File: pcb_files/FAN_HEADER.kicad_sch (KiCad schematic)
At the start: 6 parts

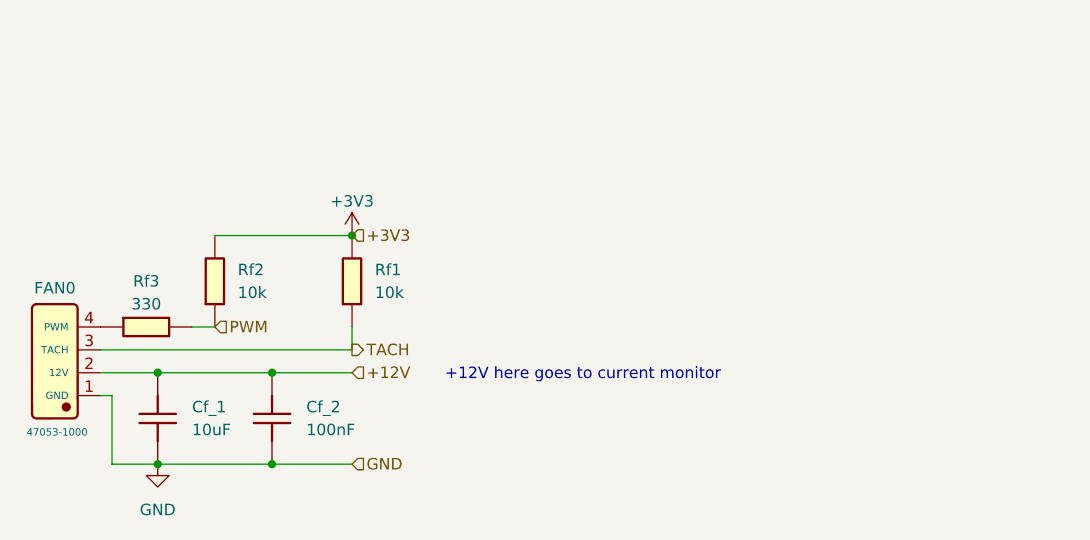
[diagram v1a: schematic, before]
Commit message: Added ESD protection to fans
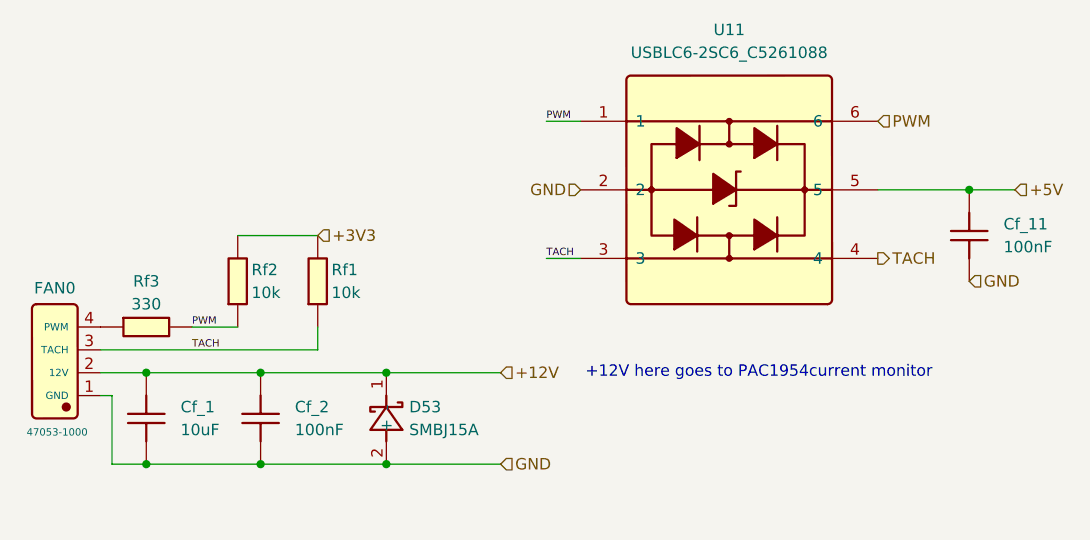
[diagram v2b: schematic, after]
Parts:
- added Cf_11: 100nF, Capacitor_SMD:C_0402_1005Metric, symbol JLCImport:CL05B104KB54PNC
- added D53: SMBJ15A, JLCImport:SMBJ15A_C42370523, symbol JLCImport:SMBJ15A_C42370523
- added U11: USBLC6-2SC6_C5261088, JLCImport:USBLC6-2SC6_C5261088, symbol JLCImport:USBLC6-2SC6_C5261088
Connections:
- net +12V: now also D53.1 (-)
- net GND: now also Cf_11.1, D53.2 (+), U11.2
- net PWM: now also U11.1, U11.6
- net TACH: now also U11.3, U11.4
- new net +5V: Cf_11.2, U11.5
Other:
- note added: "+12V here goes to PAC1954current monitor"
- note removed: "+12V here goes to current monitor"
- moved on the sheet: Cf_1, Cf_2, Rf1, Rf2
